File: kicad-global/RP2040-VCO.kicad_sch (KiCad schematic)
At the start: 51 parts, among them J1 V/oct, J2 Power Input, J3 Inv CV, J4 Out, SW1 SW_MEC_LOW_PROF_LED, SW2 SW_SP3T, U1 TL074, U2 Seed_XIAO_RP2040, U3 PDSE1-S12-S5-M-TR

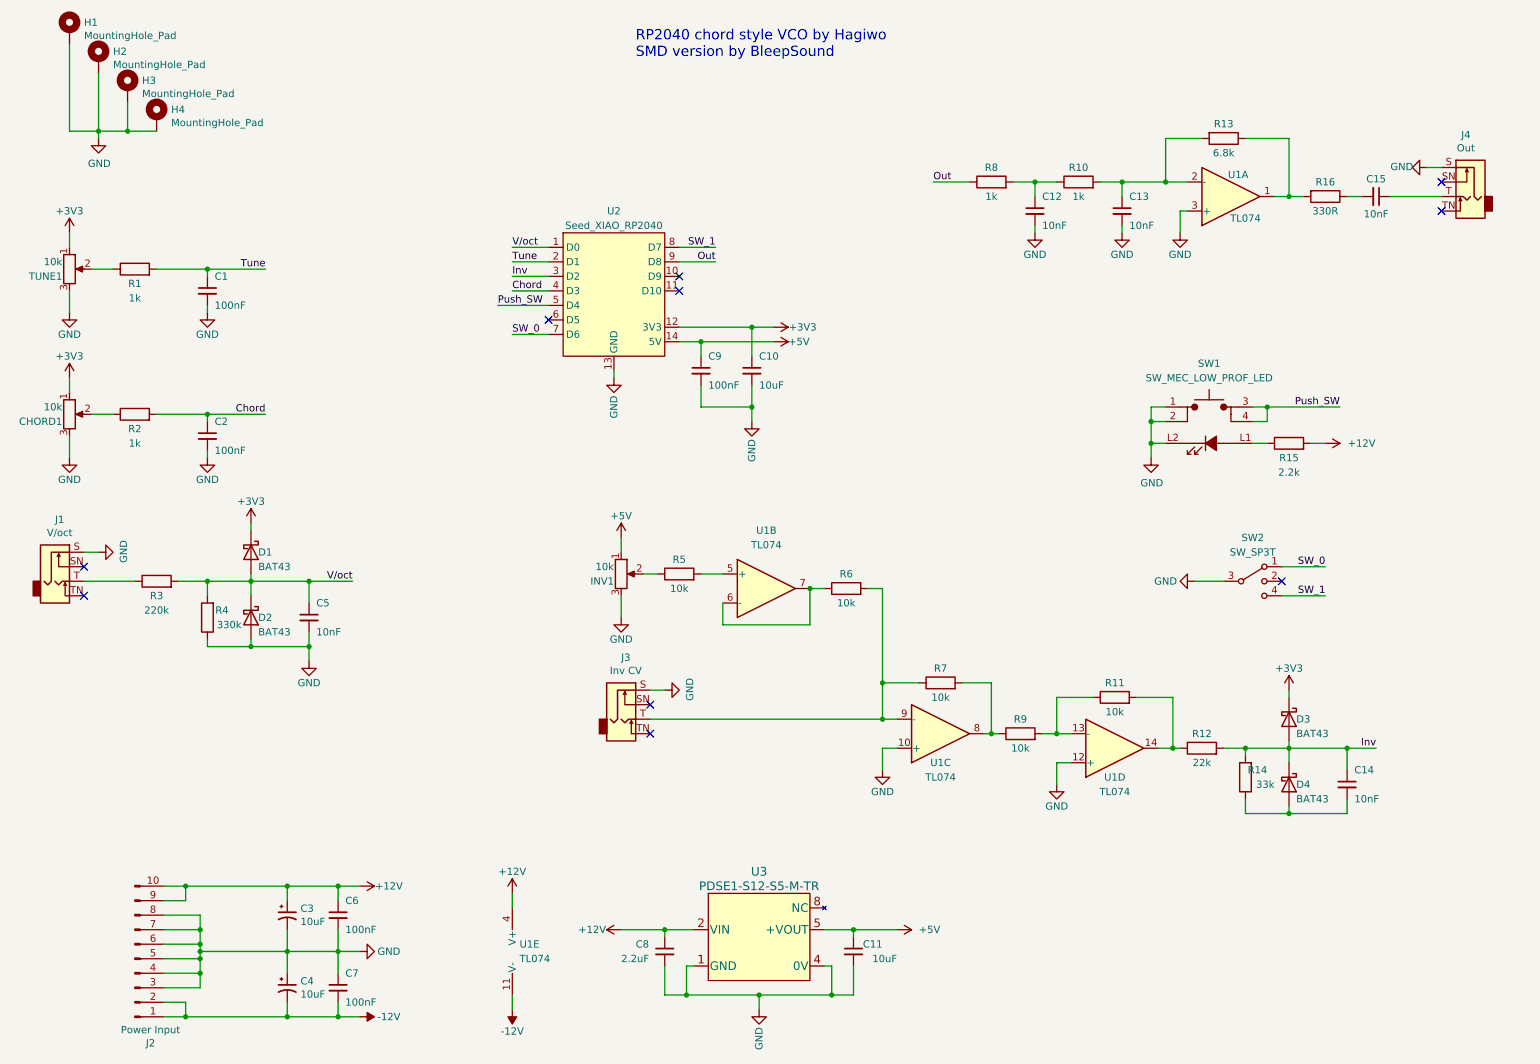
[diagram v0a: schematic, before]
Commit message: finished schem and started pcb
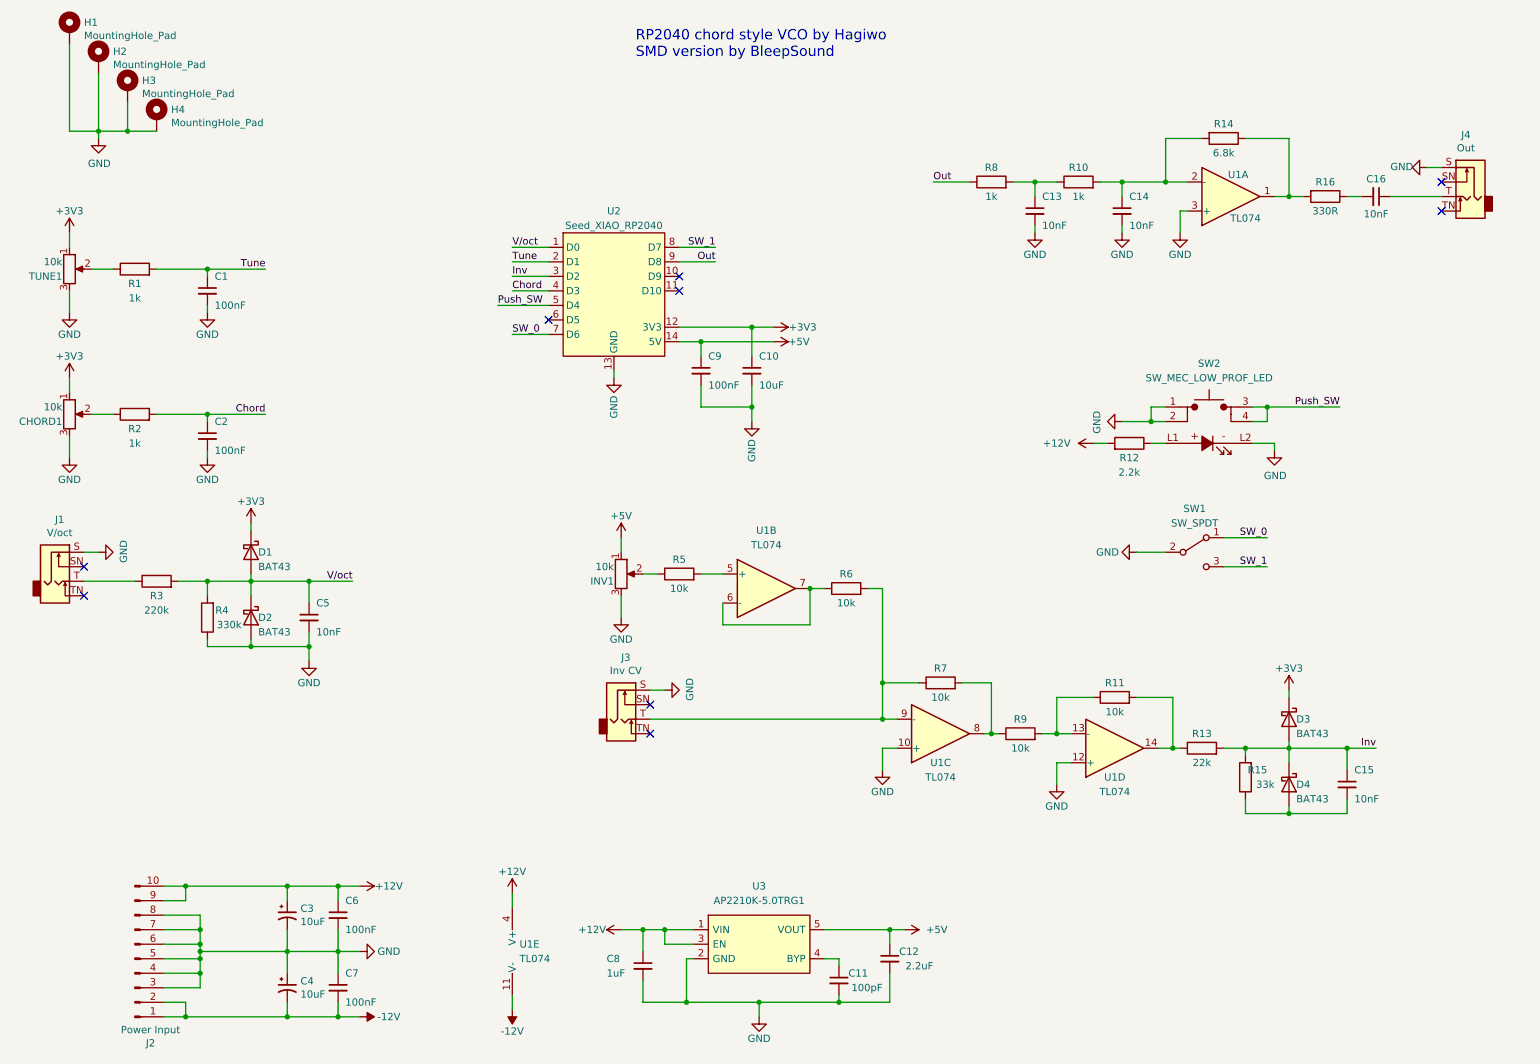
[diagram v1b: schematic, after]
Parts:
- removed SW1: SW_MEC_LOW_PROF_LED, Synth:PB01-109TL, symbol synth:SW_MEC_LOW_PROF_LED
- removed SW2: SW_SP3T, symbol Switch:SW_SP3T
- removed U3: PDSE1-S12-S5-M-TR, PDSE1-S-M_CUI, symbol Kicad_Perso:PDSE1-S12-S5-M-TR
- added C11: 100pF, Capacitor_SMD:C_0805_2012Metric_Pad1.18x1.45mm_HandSolder, symbol Device:C_Small
- added SW1: SW_SPDT, Kicad-perso:SW_Toggle_Blue_wSlots, symbol Switch:SW_SPDT
- added SW2: SW_MEC_LOW_PROF_LED, Kicad-perso:PB01-109TL, symbol Kicad_Perso:SW_MEC_LOW_PROF_LED
- added U3: AP2210K-5.0TRG1, Kicad-perso:SOT95P282X130-5N, symbol Kicad_Perso:AP2210K-5.0TRG1
- C1, C2, C6, C7, C9: Comment  (none) -> 25V 0.1uF X7R; MFN (none) -> Kemet; MFP (none) -> C0805C104M3RAC7210
- C10: Comment  (none) -> 25V 10uF 10% X5R; MFN (none) -> Samsung Electro-Mechanics; MFP (none) -> CL21A106KAYNNNE
- C12: renamed from C8; Comment  (none) -> 25V 2.2uF 10% X5R; MFN (none) -> Samsung Electro-Mechanics; MFP (none) -> CL21A225KAFNNNE
- C13: renamed from C12; Comment  (none) -> 25V 10nF 10% X7R; MFN (none) -> Samsung Electro-Mechanics; MFP (none) -> CL21B103KAANNNC
- C14: renamed from C13; Comment  (none) -> 25V 10nF 10% X7R; MFN (none) -> Samsung Electro-Mechanics; MFP (none) -> CL21B103KAANNNC
- C15: renamed from C14; Comment  (none) -> 25V 10nF 10% X7R; MFN (none) -> Samsung Electro-Mechanics; MFP (none) -> CL21B103KAANNNC
- C16: renamed from C15; Comment  (none) -> 25V 10nF 10% X7R; MFN (none) -> Samsung Electro-Mechanics; MFP (none) -> CL21B103KAANNNC
- C3, C4: footprint Capacitor_THT:CP_Radial_D5.0mm_P2.00mm -> Capacitor_SMD:CP_Elec_4x5.4; Comment  Electrolytic cap -> 25V 10uF 20%; MFN (none) -> Kemet; MFP (none) -> EXV106M025S9BAA
- C5: Comment  (none) -> 25V 10nF 10% X7R; MFN (none) -> Samsung Electro-Mechanics; MFP (none) -> CL21B103KAANNNC
- C8: renamed from C11; value 10uF -> 1uF; Comment  (none) -> 25V 1uF 10% X5R; MFN (none) -> Samsung Electro-Mechanics; MFP (none) -> CL21B105KAFNFNE
- CHORD1, INV1, TUNE1: footprint Synth:Pot-bourns-alpha -> Kicad-perso:Pot-bourns-alpha
- D1, D2, D3, D4: Comment  (none) -> 30V Schottky 0.2A; MFN (none) -> Panjit; MFP (none) -> BAT43W_R1_00001
- H1, H2, H3, H4: now left out of the parts list
- J1, J3, J4: footprint Synth:Thonkiconn -> Kicad-perso:Thonkiconn
- R1, R10, R2, R8: Comment  (none) -> 1/4W, 1%; MFN (none) -> KOA Speer; MFP (none) -> RK73H2ATTE1001F
- R11, R5, R6, R7, R9: Comment  (none) -> 1/4W, 1%; MFN (none) -> YAGEO; MFP (none) -> RC0805FR-1010KL
- R12: renamed from R15; Comment  (none) -> 1/4W, 1%; MFN (none) -> YAGEO; MFP (none) -> RC0805FR-132K2L
- R13: renamed from R12; Comment  (none) -> 1/4W, 1%; MFN (none) -> YAGEO; MFP (none) -> RC0805FR-1322KL
- R14: renamed from R13; Comment  (none) -> 1/4W, 5%; MFN (none) -> KOA Speer; MFP (none) -> RK73B2ATTDD682J
- R15: renamed from R14; Comment  (none) -> 1/4W, 1%; MFN (none) -> KOA Speer; MFP (none) -> RK73H2ATTD3302F
- R16: Comment  (none) -> 1/4W, 1%; MFN (none) -> YAGEO; MFP (none) -> RC0805FR-10330RL
- R3: Comment  (none) -> 1/4W, 1%; MFN (none) -> YAGEO; MFP (none) -> RC0805FR-13220KL
- R4: Comment  (none) -> 1/4W, 1%; MFN (none) -> KOA Speer; MFP (none) -> RK73H2ATTD3303F
- U1: MFN (none) -> Texas Instrument; MFP (none) -> TL074CDR
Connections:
- net +12V: now also C8.1, U3.1 (VIN), U3.3 (EN); no longer C12.1
- net +5V: now also C12.1, U3.5 (VOUT); no longer C8.1
- net GND: now also C11.2, SW1.2 (B), SW2.1, SW2.2, SW2.L2, U3.2 (GND)
- net Push_SW: now also SW2.3, SW2.4
- net SW_0: now also SW1.1 (A)
- net SW_1: now also SW1.3 (C)
- net at R12.1: now also SW2.L1
- new net: C11.1, U3.4 (BYP)
- no-connect marks 10 -> 9
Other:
- moved on the sheet: C12, C8, R12

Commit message: update schem + begin routing
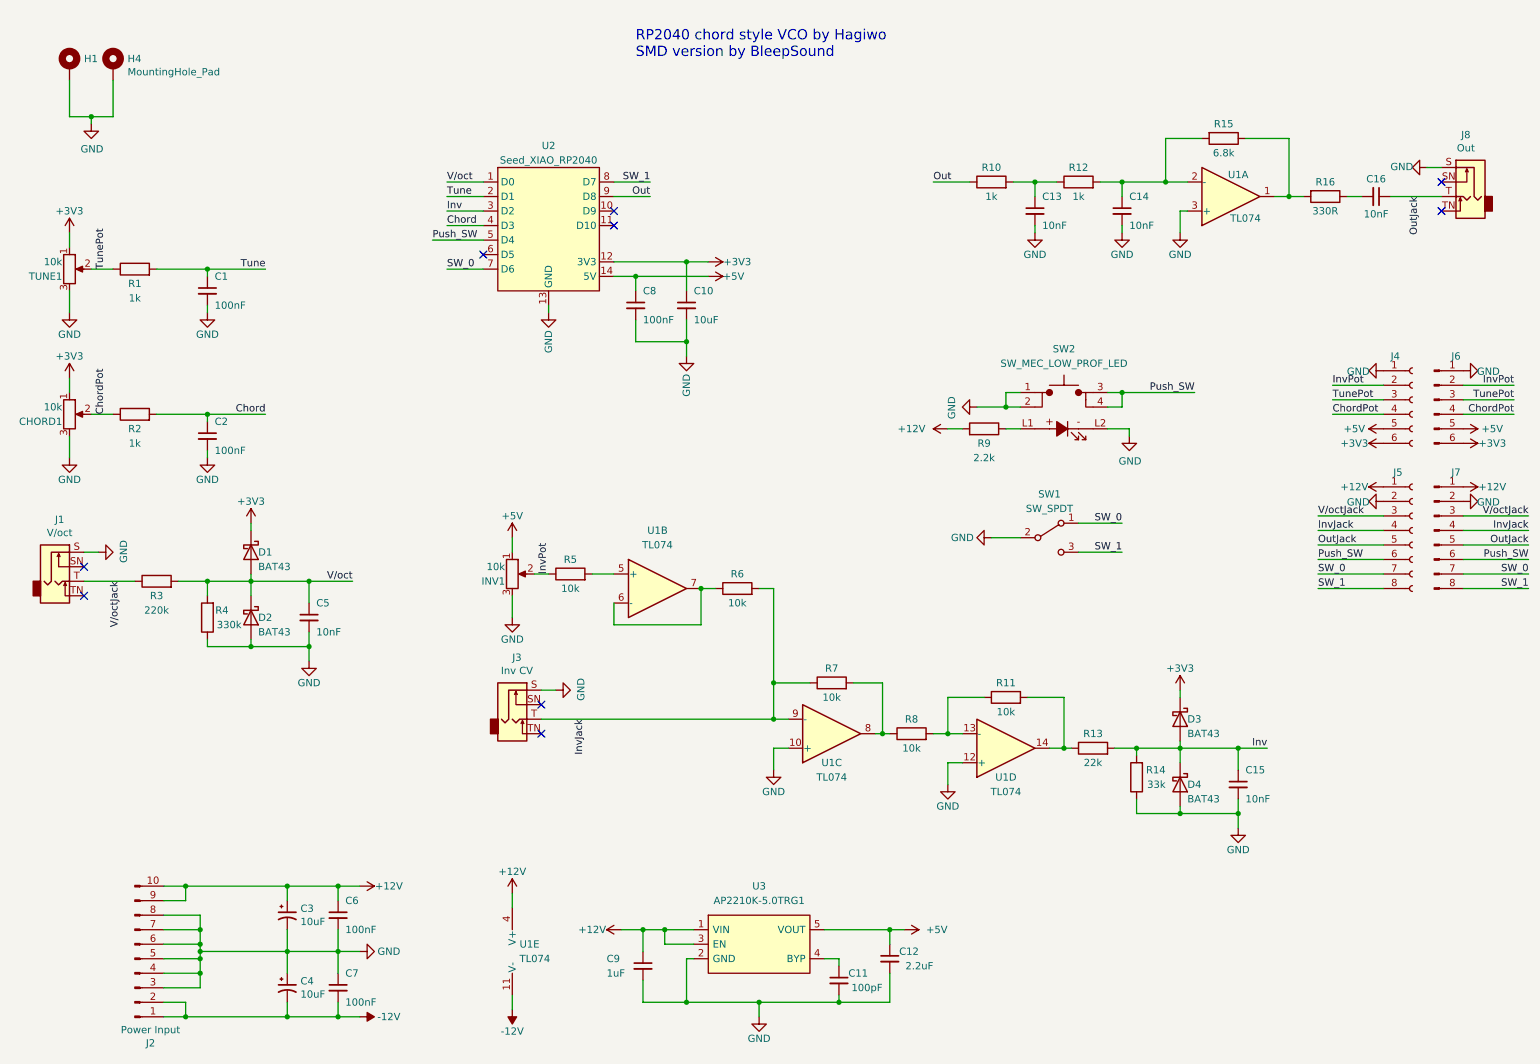
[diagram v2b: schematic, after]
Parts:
- removed H2, H3: MountingHole_Pad, Synth:Doepfer Mounting hole, symbol Mechanical:MountingHole_Pad
- added J4: Conn_01x06_Female, Connector_PinSocket_2.54mm:PinSocket_1x06_P2.54mm_Vertical, symbol Connector:Conn_01x06_Female
- added J5: Conn_01x08_Female, Connector_PinSocket_2.54mm:PinSocket_1x08_P2.54mm_Vertical, symbol Connector:Conn_01x08_Female
- added J6: Conn_01x06_Male, Connector_PinHeader_2.54mm:PinHeader_1x06_P2.54mm_Horizontal, symbol Connector:Conn_01x06_Male
- added J7: Conn_01x08_Male, Connector_PinHeader_2.54mm:PinHeader_1x08_P2.54mm_Horizontal, symbol Connector:Conn_01x08_Male
- renumbered C9 to C8, C8 to C9, J4 to J8, R8 to R10, R10 to R12, R15 to R14, R14 to R15, R9 to R8, R12 to R9
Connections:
- net +12V: now also J5.1 (Pin_1), J7.1 (Pin_1)
- net +3V3: now also J4.6 (Pin_6), J6.6 (Pin_6)
- net +5V: now also J4.5 (Pin_5), J6.5 (Pin_5)
- net GND: now also C15.2, D4.2 (A), R14.1, J4.1 (Pin_1), J5.2 (Pin_2), J6.1 (Pin_1), J7.2 (Pin_2)
- net Push_SW: now also J5.6 (Pin_6), J7.6 (Pin_6)
- net SW_0: now also J5.7 (Pin_7), J7.7 (Pin_7)
- net SW_1: now also J5.8 (Pin_8), J7.8 (Pin_8)
- net TunePot: now reaches R1.1, TUNE1.2
- net TunePot: now also J4.3 (Pin_3), J6.3 (Pin_3)
- net InvJack: now reaches J3.T, R6.2, R7.1, U1.9 (-)
- net InvJack: now also J5.4 (Pin_4), J7.4 (Pin_4)
- net OutJack: now reaches C16.1, J8.T
- net OutJack: now also J5.5 (Pin_5), J7.5 (Pin_5)
- net V/octJack: now reaches J1.T, R3.1
- net V/octJack: now also J5.3 (Pin_3), J7.3 (Pin_3)
- net ChordPot: now reaches CHORD1.2, R2.1
- net ChordPot: now also J4.4 (Pin_4), J6.4 (Pin_4)
- net InvPot: now reaches INV1.2, R5.1
- net InvPot: now also J4.2 (Pin_2), J6.2 (Pin_2)
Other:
- moved on the sheet: C10, C15, C8, D3, D4, H1, H4, INV1, J3, R11, R13, R14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

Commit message: Routing finished
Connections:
- net +12V: now also J5.8 (Pin_8), J7.8 (Pin_8); no longer J5.1 (Pin_1), J7.1 (Pin_1)
- net GND: now also J5.4 (Pin_4), J7.4 (Pin_4); no longer J5.2 (Pin_2), J7.2 (Pin_2)
- net InvJack: now also J5.2 (Pin_2), J7.2 (Pin_2); no longer J5.4 (Pin_4), J7.4 (Pin_4)
- net OutJack: now also J5.1 (Pin_1), J7.1 (Pin_1); no longer J5.5 (Pin_5), J7.5 (Pin_5)
- net SW_0: now also J5.5 (Pin_5), J7.5 (Pin_5); no longer J5.7 (Pin_7), J7.7 (Pin_7)
- net SW_1: now also J5.7 (Pin_7), J7.7 (Pin_7); no longer J5.8 (Pin_8), J7.8 (Pin_8)

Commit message: update to v1.1
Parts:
- added H1, H2: SpacerHoles, MountingHole:MountingHole_3.2mm_M3, symbol Mechanical:MountingHole
- D1, D2, D3, D4: footprint Diode_SMD:D_SOD-123 -> Kicad-perso:D_SOD-123
- J3: renamed from J6; footprint Connector_PinHeader_2.54mm:PinHeader_1x06_P2.54mm_Horizontal -> Connector_PinHeader_2.54mm:PinHeader_1x06_P2.54mm_Vertical
- J5: renamed from J7; footprint Connector_PinHeader_2.54mm:PinHeader_1x08_P2.54mm_Horizontal -> Connector_PinHeader_2.54mm:PinHeader_1x08_P2.54mm_Vertical
- U1: footprint Package_SO:SOIC-14_3.9x8.7mm_P1.27mm -> Kicad-perso:SOIC-14_3.9x8.7mm_P1.27mm
- renumbered C16 to C1, C3 to C10, C6 to C11, C9 to C13, C11 to C14, C4 to C15, C7 to C16, C13 to C2, C14 to C3, C1 to C4, C8 to C5, C10 to C6, C2 to C7, C5 to C8, C15 to C9, H1 to H3, J8 to J1, J4 to J2, J5 to J4, J1 to J6, J3 to J7, J2 to J8, R15 to R1, R6 to R10, R4 to R11, R7 to R12, R11 to R13, R8 to R14, R13 to R15, R14 to R16, R10 to R2, R12 to R3, R16 to R4, R1 to R5, R2 to R6, R9 to R7, R5 to R8, R3 to R9, SW2 to SW1, SW1 to SW2

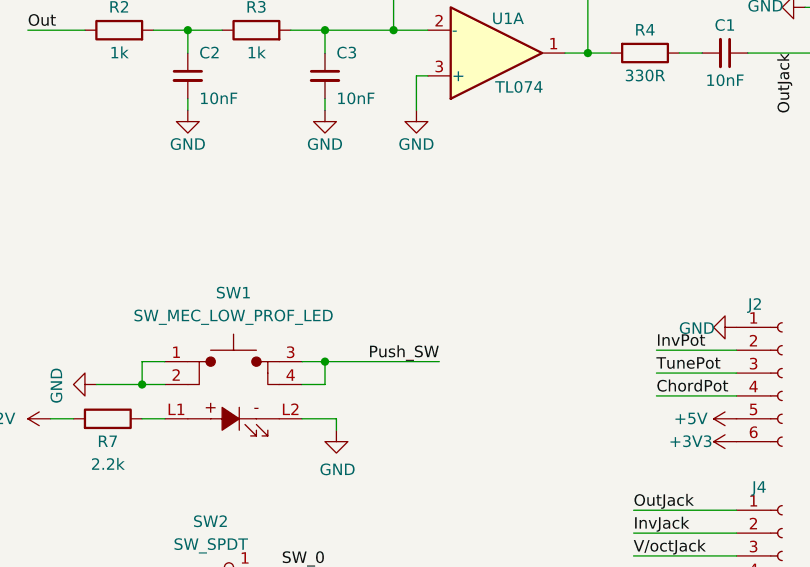
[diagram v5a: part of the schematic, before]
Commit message: update board with pullup on switch
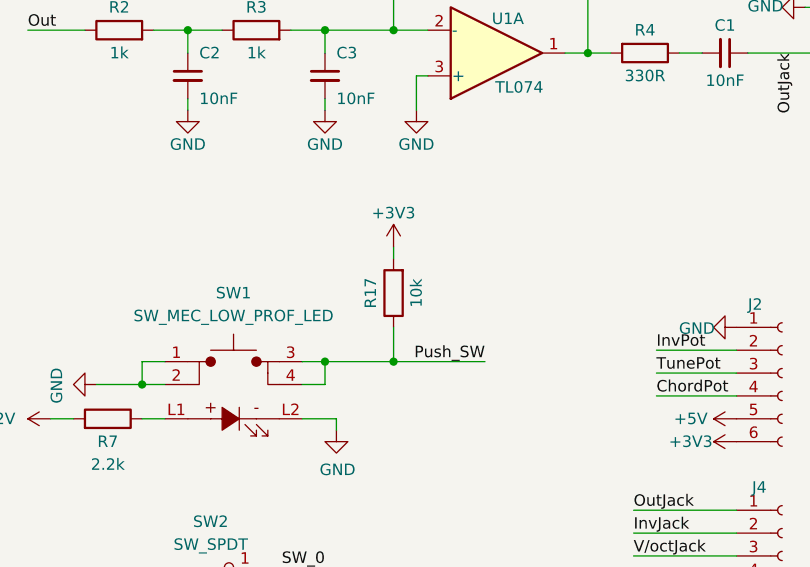
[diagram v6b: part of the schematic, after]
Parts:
- added R17: 10k, Resistor_SMD:R_0805_2012Metric_Pad1.20x1.40mm_HandSolder, symbol Device:R
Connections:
- net +3V3: now also R17.2
- net Push_SW: now also R17.1
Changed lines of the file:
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@@
   (junction (at 143.51 187.96) (diameter 0) (color 0 0 0 0)
   )
+  (junction (at 214.63 81.28) (diameter 0) (color 0 0 0 0)
+  )
   (junction (at 130.81 58.42) (diameter 0) (color 0 0 0 0)
   )
@@
     (stroke (width 0) (type default))
   )
+  (wire (pts (xy 214.63 68.58) (xy 214.63 69.85))
+    (stroke (width 0) (type default))
+  )
   (wire (pts (xy 143.51 115.57) (xy 146.05 115.57))
     (stroke (width 0) (type default))
@@
     (stroke (width 0) (type default))
   )
-  (wire (pts (xy 207.01 81.28) (xy 219.71 81.28))
+  (wire (pts (xy 207.01 81.28) (xy 214.63 81.28))
     (stroke (width 0) (type default))
   )
@@
     (stroke (width 0) (type default))
   )
+  (wire (pts (xy 214.63 81.28) (xy 224.79 81.28))
+    (stroke (width 0) (type default))
+  )
   (wire (pts (xy 39.37 182.88) (xy 45.72 182.88))
     (stroke (width 0) (type default))
@@
     (stroke (width 0) (type default))
   )
+  (wire (pts (xy 214.63 77.47) (xy 214.63 81.28))
+    (stroke (width 0) (type default))
+  )
   (wire (pts (xy 236.22 46.99) (xy 236.22 36.83))
     (stroke (width 0) (type default))
@@
     (effects (font (size 1.27 1.27)) (justify left bottom))
   )
-  (label "Push_SW" (at 219.71 81.28 180) (fields_autoplaced)
+  (label "Push_SW" (at 224.79 81.28 180) (fields_autoplaced)
     (effects (font (size 1.27 1.27)) (justify right bottom))
   )
@@
     )
   )
+  (symbol (lib_id "Device:R") (at 214.63 73.66 180) (unit 1)
+    (in_bom yes) (on_board yes) (dnp no)
+    (property "Reference" "R17" (at 212.09 73.66 90)
+      (effects (font (size 1.27 1.27)))
+    )
+    (property "Value" "10k" (at 217.17 73.66 90)
+      (effects (font (size 1.27 1.27)))
+    )
+    (property "Footprint" "Resistor_SMD:R_0805_2012Metric_Pad1.20x1.40mm_HandSolder" (at 216.408 73.66 90)
+      (effects (font (size 1.27 1.27)) hide)
+    )
+    (property "Datasheet" "~" (at 214.63 73.66 0)
+      (effects (font (size 1.27 1.27)) hide)
+    )
+    (property "Comment " "1/4W, 1%" (at 214.63 73.66 0)
+      (effects (font (size 1.27 1.27)) hide)
+    )
+    (property "MFN" "YAGEO" (at 214.63 73.66 0)
+      (effects (font (size 1.27 1.27)) hide)
+    )
+    (property "MFP" "RC0805FR-1010KL" (at 214.63 73.66 0)
+      (effects (font (size 1.27 1.27)) hide)
+    )
+    (pin "1")
+    (pin "2")
+    (instances
+      (project "RP2040-VCO"
+        (path "/fea7c5d1-76d6-41a0-b5e3-29889dbb8ce0"
+          (reference "R17") (unit 1)
+        )
+      )
+    )
+  )
   (symbol (lib_id "power:+12V") (at 100.33 168.91 0) (unit 1)
     (in_bom yes) (on_board yes) (dnp no)
@@
         )
       )
+    )
+  )
+  (symbol (lib_id "power:+3V3") (at 214.63 68.58 0) (unit 1)
+    (in_bom yes) (on_board yes) (dnp no)
+    (property "Reference" "#PWR048" (at 214.63 72.39 0)
+      (effects (font (size 1.27 1.27)) hide)
+    )
+    (property "Value" "+3V3" (at 214.63 64.77 0)
+      (effects (font (size 1.27 1.27)))
+    )
+    (property "Footprint" "" (at 214.63 68.58 0)
+      (effects (font (size 1.27 1.27)) hide)
+    )
+    (property "Datasheet" "" (at 214.63 68.58 0)
+      (effects (font (size 1.27 1.27)) hide)
+    )
+    (pin "1")
+    (instances
+      (project "RP2040-VCO"
+        (path "/fea7c5d1-76d6-41a0-b5e3-29889dbb8ce0"
+          (reference "#PWR048") (unit 1)
+        )
+      )
